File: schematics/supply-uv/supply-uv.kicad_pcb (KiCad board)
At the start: 2 copper layers, 150 x 200 mm, 284 parts, among them J1 VSYS connector to Board#2, J2 power +5V connector to board#2, J3 +5V_PWR (with fuse), J4 PWR_OUT (with fuse), J5 CW2B-10A-T, J6 USBASP, J7 JST XH B3B, K1 SRD-12VDC-SL-C, Q1 5N65F, Q10 STP13NK60Z, Q11 STP13NK60Z, Q12 IRLML0030, Q13 IRLML0030, Q14 IRLML0030, Q2 IRLML5203, Q3 IRLML5203, Q4 IRLML5203, Q5 STP13NK60Z, Q6 STP13NK60Z, Q7 IRLML0030, Q8 IRLML5203, Q9 IRLML0030, SW1 SW_Push, U1 ISO1540, U10 TL331, U11 EL817, U12 UC3525, U13 IRS21867S, U14 TL432DBZ, U15 EL817, U16 UC3525, U17 OP213ESZ, U18 IRS21867S, U19 EL817, U2 R7731, U20 INA169, U21 TL431DBZ, U22 ATtiny1616-M, U3 EL817, U4 EL817, U5 L7805ABV, U6 L7805ABV, U7 TL431DBZ, U8 EL817, U9 TL432DBZ, Y1 B32022A3223M000

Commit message: first board routed
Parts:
- added H2: MountingHole, MountingHole:MountingHole_2.2mm_M2, F.Cu at (143.1, 109.0)
- added H3: MountingHole, MountingHole:MountingHole_2.2mm_M2, F.Cu at (105.1, 120.0)
- added H4: MountingHole, MountingHole:MountingHole_2.2mm_M2, F.Cu at (35.1, 116.0)
- added H5: MountingHole, MountingHole:MountingHole_2.2mm_M2, F.Cu at (68.1, 87.0)
- added H6: MountingHole, MountingHole:MountingHole_2.2mm_M2, F.Cu at (127.1, 151.0)
- added H7: MountingHole, MountingHole:MountingHole_2.2mm_M2, F.Cu at (73.1, 163.0)
- moved H1 532.3 mm to (101.1, 245.0)

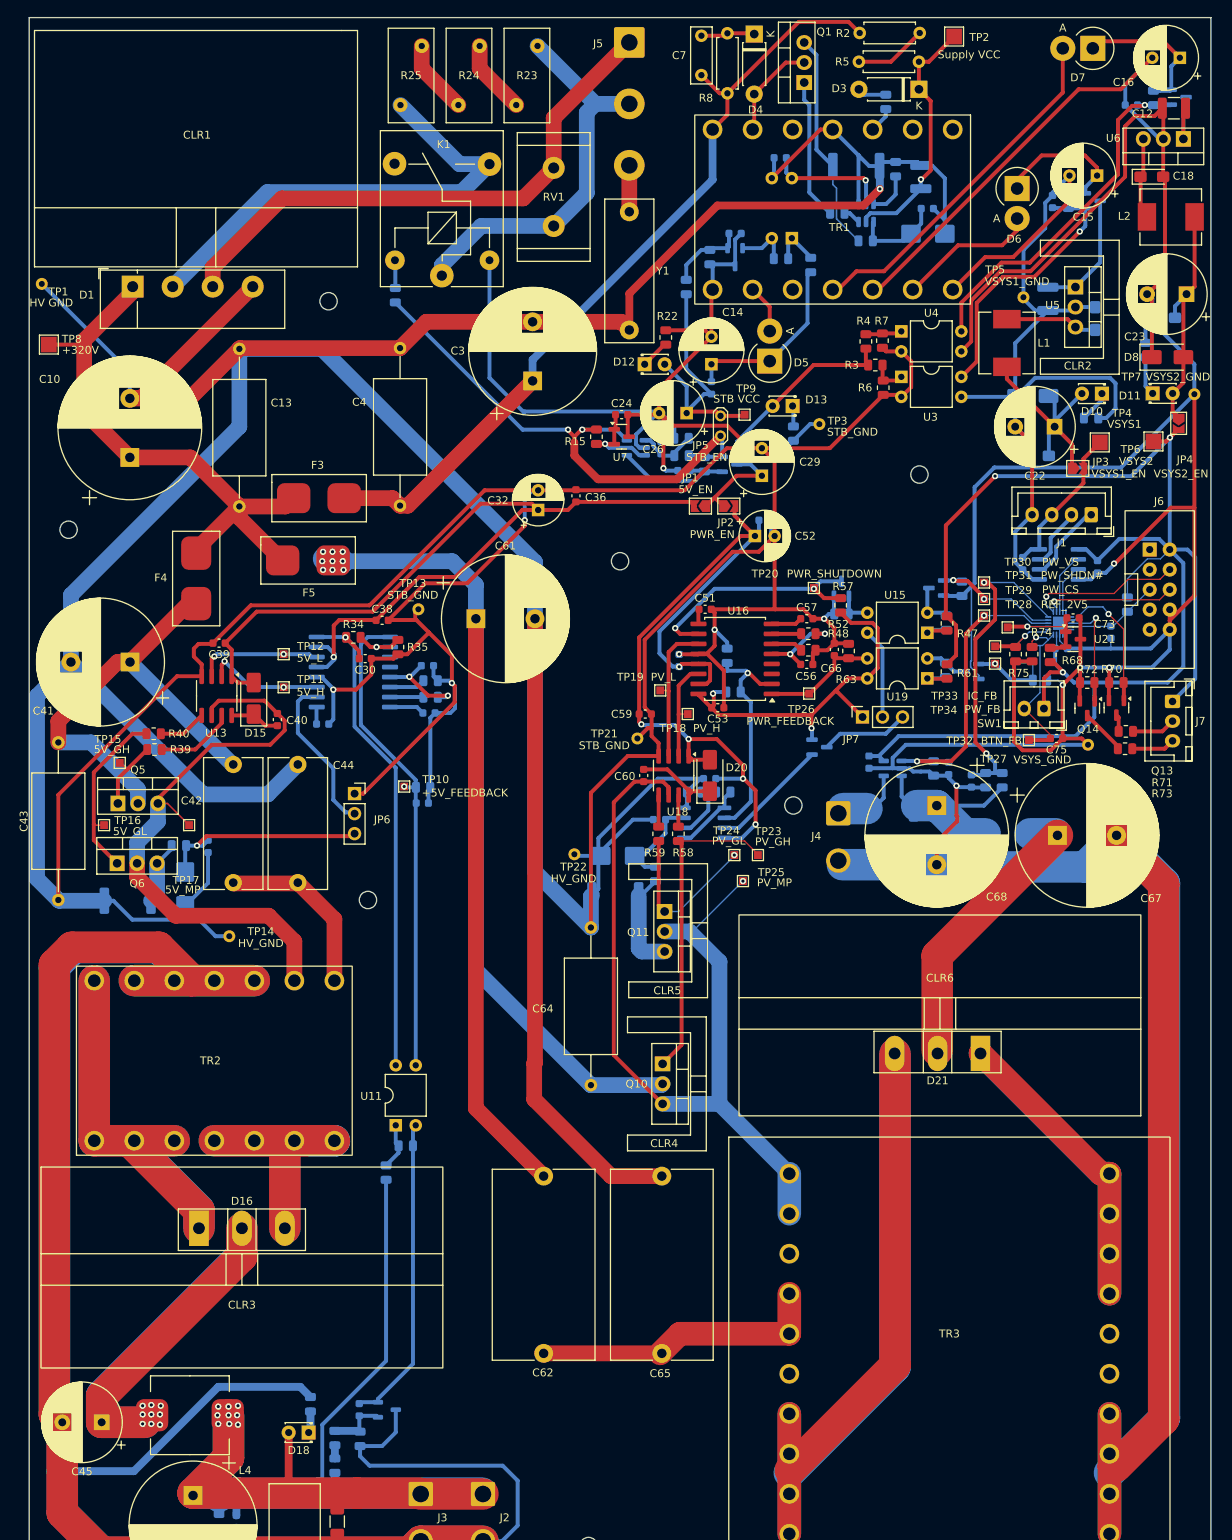
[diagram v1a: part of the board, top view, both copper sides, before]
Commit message: some changes in board routing
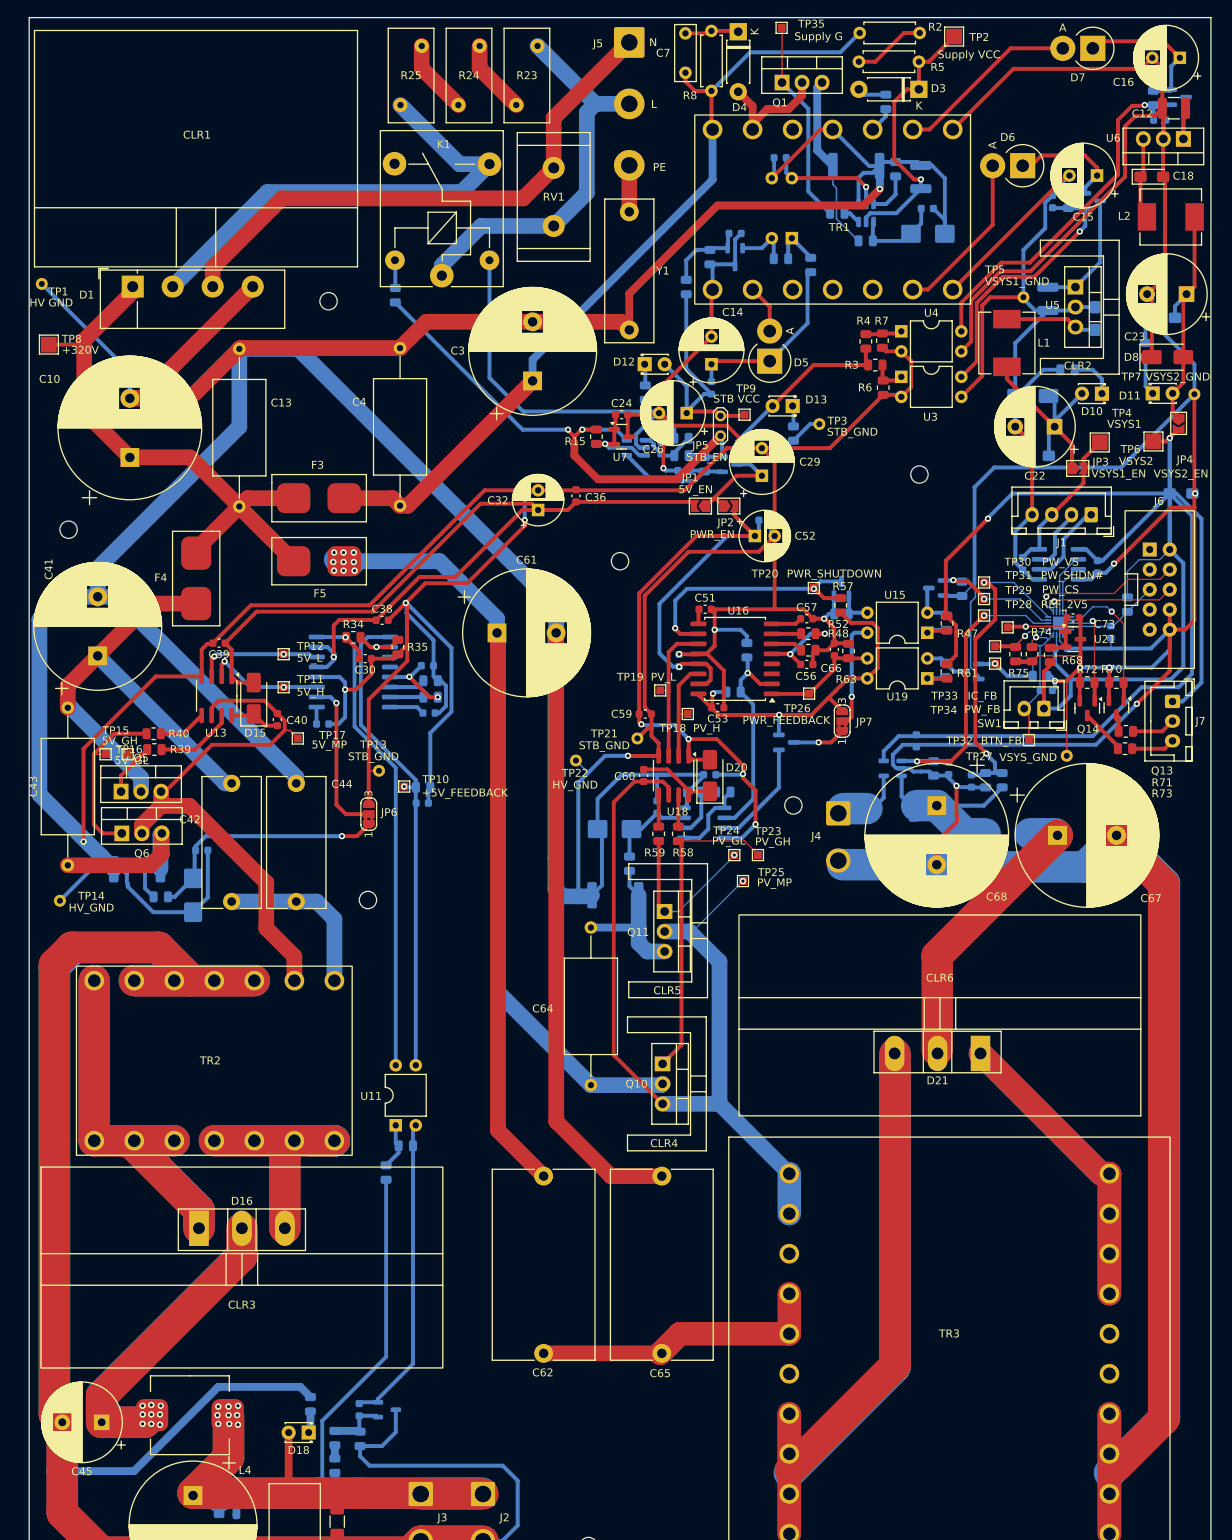
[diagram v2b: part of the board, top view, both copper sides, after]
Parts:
- added C76: 22 uF, Capacitor_Tantalum_SMD:CP_EIA-3216-10_Kemet-I_Pad1.58x1.35mm_HandSolder, B.Cu at (176.3, 111.4)
- added TP35: Supply G, TestPoint:TestPoint_Pad_1.0x1.0mm, F.Cu at (125.6, 52.3)
- C75, R22: moved to B.Cu
- JP6, JP7: footprint Connector_PinSocket_2.54mm:PinSocket_1x03_P2.54mm_Vertical -> Jumper:SolderJumper-3_P1.3mm_Bridged2Bar12_RoundedPad1.0x1.5mm_NumberLabels
- moved TP14 22.0 mm to (34.0, 163.1)
- moved TP13 21.1 mm to (74.5, 146.6)
- moved TP17 17.6 mm to (64.2, 142.5)
- moved TP22 11.9 mm to (99.5, 145.3)
- moved TP16 9.00 mm to (39.8, 144.5)
- moved R22 7.47 mm to (108.3, 98.6), turned to 90 degrees
- moved R32 6.89 mm to (46.8, 162.6)
- moved R18 6.82 mm to (161.9, 95.7), turned to 0 degrees
- moved C71 6.58 mm to (142.7, 142.8)
- moved C75 6.24 mm to (159.2, 136.4)
- moved C43 4.56 mm to (35.0, 158.6)
- moved Q8 4.24 mm to (126.2, 143.0)
- moved R41 4.18 mm to (43.8, 159.1)
- moved C41 4.17 mm to (38.8, 132.0), turned to 90 degrees
- moved C9 4.07 mm to (173.6, 64.0), turned to 180 degrees
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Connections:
- C43 pad 1: /5V_PWR Sheet/HV_GND -> /5V_PWR Sheet/DCDC_CURRENT_SENSE
- C64 pad 1: /5V_PWR Sheet/HV_GND -> /pwrout Sheet/DCDC_CURRENT_SENSE
- JP6 pad 1: /5V_PWR Sheet/STB_GND -> Net-(D14-A2)
- JP6 pad 3: Net-(D14-A2) -> /5V_PWR Sheet/STB_GND
- JP7 pad 1: /pwrout Sheet/DCDC_5V_VREF -> Net-(JP7-A)
- JP7 pad 3: Net-(JP7-B) -> /pwrout Sheet/DCDC_5V_VREF
- Q8 pad 3: Net-(JP7-B) -> Net-(JP7-A)
- TR1 pad 1: (no net) -> /VSYS_PWR_GND
- TR1 pad 3: (no net) -> Net-(D7-A)
- TR1 pad 6: /VSYS_PWR_GND -> (no net)
- TR1 pad 8: Net-(D7-A) -> (no net)
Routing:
- net /VSYS_PWR_VCC: track 197.2 -> 253.4 mm, vias 3 -> 2
- net /5V_PWR Sheet/HV_GND: track 648.0 -> 624.5 mm, vias 1 -> 3
- net Net-(D7-A): track 44.5 -> 23.3 mm
- net /5V_PWR Sheet/STB_GND: track 454.0 -> 472.1 mm
- net /5V_PWR Sheet/DCDC_CURRENT_SENSE: track 7.69 -> 25.5 mm
- net /VSYS_PWR_GND: track 385.2 -> 372.4 mm, vias 4 -> 6
- net Net-(JP7-B): track 11.2 -> 0.00 mm
- net Net-(Q1-G): track 18.0 -> 26.1 mm
- net Net-(JP7-A): track 0.00 -> 6.74 mm, vias 0 -> 1
- net /pwrout Sheet/DCDC_CURRENT_SENSE: track 12.7 -> 19.5 mm
- net Net-(Q1-S): track 28.0 -> 22.5 mm
- net /pwrout Sheet/STB_VCC: track 104.9 -> 110.1 mm
- net /pwrout Sheet/HV_VCC_FUSE: track 174.9 -> 169.7 mm
- net Net-(D14-A2): track 26.5 -> 31.5 mm
- net Net-(Q5-S): track 76.4 -> 72.2 mm
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
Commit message: Boards prepared to order
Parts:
- added TP3: Supply GND, Library:TestPoint_Plated_Hole_D1.0mm, F.Cu at (131.7, 89.1)
- C56: renamed from C55; moved to F.Cu
- TP10: renamed from TP8; footprint TestPoint:TestPoint_Pad_2.0x2.0mm -> TestPoint:TestPoint_Pad_1.0x1.0mm
- TP2: footprint TestPoint:TestPoint_Pad_2.0x2.0mm -> TestPoint:TestPoint_Pad_1.0x1.0mm
- TP5: renamed from TP4; footprint TestPoint:TestPoint_Pad_2.0x2.0mm -> TestPoint:TestPoint_Pad_1.0x1.0mm
- TP7: renamed from TP6; footprint TestPoint:TestPoint_Pad_2.0x2.0mm -> TestPoint:TestPoint_Pad_1.0x1.0mm
- moved C56 2.30 mm to (123.5, 112.5)
- renumbered C76 to C27, C27 to C28, C28 to C29, C29 to C30, C30 to C31, C31 to C32, C32 to C33, C33 to C34, C34 to C35, C35 to C36, C36 to C37, C37 to C38, C38 to C39, C39 to C40, C40 to C41, C41 to C42, C42 to C43, C43 to C45, C45 to C46, C46 to C47, C47 to C48, C48 to C49, C49 to C50, C50 to C51, C51 to C52, C52 to C53, C53 to C54, C54 to C55, C56 to C57, C57 to C58, C58 to C59, C59 to C60, C60 to C61, C61 to C62, C62 to C63, C63 to C64, C64 to C66, C66 to C67, C67 to C68, C68 to C69, C69 to C70, C70 to C71, C71 to C72, C72 to C73, C73 to C74, C74 to C75, C75 to C76, R9 to R8, R8 to R9, TP9 to TP11, TP10 to TP12, TP11 to TP13, TP12 to TP14, TP13 to TP15, TP14 to TP16, TP15 to TP17, TP16 to TP18, TP17 to TP19, TP18 to TP20, TP19 to TP21, TP20 to TP22, TP21 to TP23, TP22 to TP24, TP23 to TP25, TP24 to TP26, TP25 to TP27, TP26 to TP28, TP27 to TP29, TP28 to TP30, TP29 to TP31, TP30 to TP32, TP31 to TP33, TP32 to TP34, TP33 to TP35, TP34 to TP36, TP3 to TP4, TP5 to TP6, TP7 to TP8, TP35 to TP9
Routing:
- net /5V_PWR Sheet/HV_GND: track 624.5 -> 638.1 mm
- net /5V_PWR Sheet/STB_GND: track 472.1 -> 477.7 mm
- net /standby Sheet/V_STANDBY_PRE: track 70.4 -> 73.7 mm
- net Net-(D2-A1): track 10.1 -> 13.0 mm
- net Net-(D12-A): track 32.6 -> 34.0 mm
- net Net-(Q5-S): track 72.2 -> 71.0 mm
- net /standby Sheet/VSYS1_PRE_VCC: track 16.6 -> 15.5 mm
- net Net-(D5-K): track 22.7 -> 23.7 mm
- net /VSYS_PWR_VCC: track 253.4 -> 252.4 mm
- net /pwrout Sheet/STB_VCC: track 110.1 -> 110.8 mm
- net Net-(D4-A): track 15.7 -> 15.0 mm
